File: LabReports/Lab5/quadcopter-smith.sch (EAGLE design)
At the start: 58 parts, among them J1 AVR_SPI_PRG_6NS, Q1 SI2302CDS, Q2 SI2302CDS, Q3 SI2302CDS, Q4 SI2302CDS, U1 ATMEGA128RFA1, U2 LSM9DS0-LGA24, Y1 16MHz

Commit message: Added grouping names and separators to schematic
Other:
- note added: "IMU (and bypass caps)"
- note added: "Microcontroller (and bypass caps, status LEDs)"
- note added: "Motor Controllers (and orientation LEDs)"
- note added: "Power Supply"
- note added: "Serial Headers"
- moved on the sheet: B1, C1, C10, C11, C12, C13, C14, C15, C16, C17, C18, C2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

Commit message: Beautified schematic
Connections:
- net VCC renamed VBAT
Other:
- note added: "Bypass Caps (place near supply pins)"
- note added: "IMU"
- note added: "Microcontroller"
- note added: "Motor Controllers"
- note added: "Orientation LEDs"
- note added: "Status LEDs"
- note added: "Trevor Smith and David Smith"
- note removed: "IMU (and bypass caps)"
- note removed: "Microcontroller (and bypass caps, status LEDs)"
- note removed: "Motor Controllers (and orientation LEDs)"
- moved on the sheet: B1, C1, C11, C12, C13, C14, C15, C16, C17, C18, C2, C3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

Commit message: Added design review of Dejun and Ryan
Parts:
- C3, C4: value 1mF -> 1uF
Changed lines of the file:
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@@
 <setting verticaltext="up"/>
 </settings>
-<grid distance="0.1" unitdist="inch" unit="inch" style="lines" multiple="1" display="no" altdistance="0.05" altunitdist="inch" altunit="inch"/>
+<grid distance="0.1" unitdist="inch" unit="inch" style="lines" multiple="1" display="no" altdistance="0.01" altunitdist="inch" altunit="inch"/>
 <layers>
 <layer number="1" name="Top" color="4" fill="1" visible="no" active="no"/>
@@
 <part name="GND1" library="Lab5" deviceset="GND" device=""/>
 <part name="GND2" library="Lab5" deviceset="GND" device=""/>
-<part name="C3" library="Lab5" deviceset="C-US" device="C0805" value="1mF"/>
-<part name="C4" library="Lab5" deviceset="C-US" device="C0805" value="1mF"/>
+<part name="C3" library="Lab5" deviceset="C-US" device="C0805" value="1uF"/>
+<part name="C4" library="Lab5" deviceset="C-US" device="C0805" value="1uF"/>
 <part name="GND3" library="Lab5" deviceset="GND" device=""/>
 <part name="GND4" library="Lab5" deviceset="GND" device=""/>

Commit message: modified schem after design review
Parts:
- removed C6, C7: JUMP, Lab5:C-USC0805
- added R12, R13, R14: 10k, Trevor-lab4:RESISTOR-0805
- added R15, R16: JUMP, Lab5:R-US_R0805
- LED1, LED2: value GREEN -> BLUE
- LED4, LED6: value (none) -> GREEN
- LED5, LED7: value (none) -> RED
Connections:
- removed net 3.3V: C10.1, C13.1, C17.1, C18.1, C9.1, R1.2, R10.2, R11.2, R4.2, R9.2, U$2.OUT, U1.DEVDD, U1.EVDD, U2.CS_G, U2.CS_XM, U2.DEN_G, U2.SDO_G/SA0_G, U2.SDO_XM/SA0_XM, U2.VDD_1, U2.VDD_2, U2.VDD_3, U2.VDD_IO
- new net 3V: C10.1, C13.1, C17.1, C18.1, C9.1, R1.2, R10.2, R11.2, R12.P$1, R13.P$1, R14.P$1, R4.2, R9.2, U$2.OUT, U1.DEVDD, U1.EVDD, U2.VDD_1, U2.VDD_2, U2.VDD_3, U2.VDD_IO
- new net N$27: R12.P$2, U2.CS_G
- new net N$28: R13.P$2, U2.CS_XM
- new net N$29: R14.P$2, U2.DEN_G
- net GND: now also U2.SDO_G/SA0_G, U2.SDO_XM/SA0_XM
- net N$5: now also R16.1; no longer C7.2
- net N$6: now also R15.1; no longer C6.2
- net N$7: now also R15.2; no longer C6.1
- net N$8: now also R16.2; no longer C7.1
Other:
- note added: "For easily identifying the orientation of the quadcopter when it is flying"

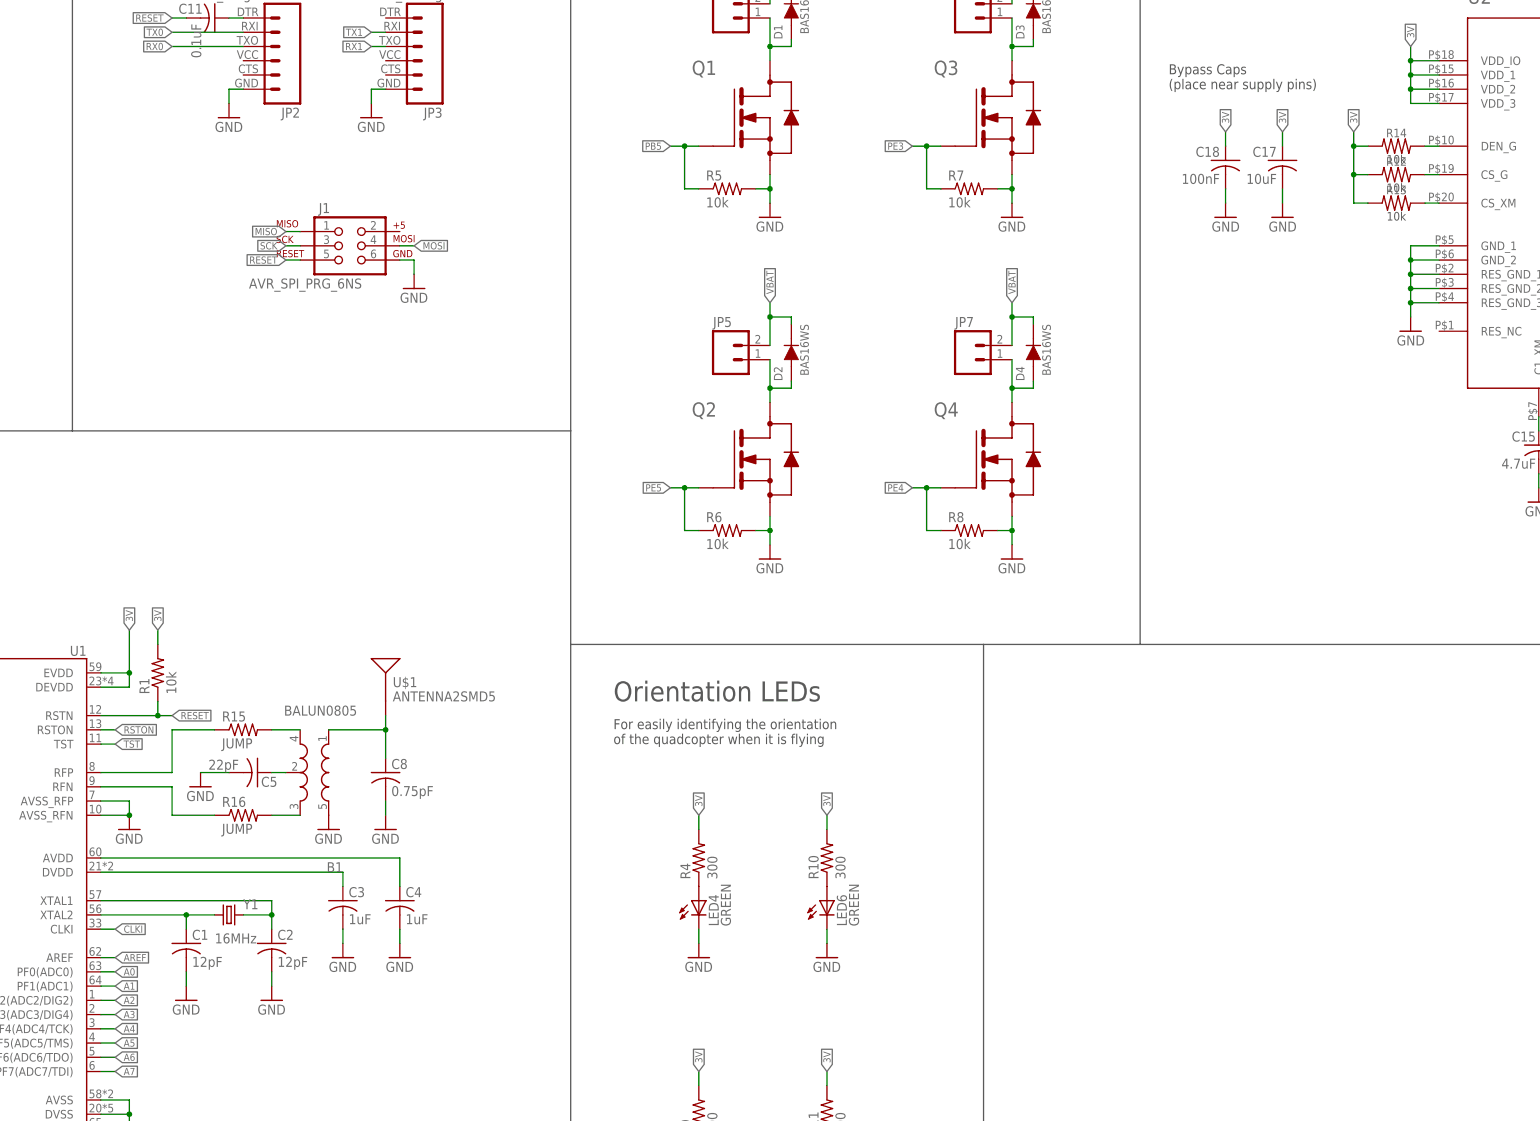
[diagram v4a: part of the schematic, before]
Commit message: removed jumpers on balun circuit, connected tst and clki on atmega to gnd
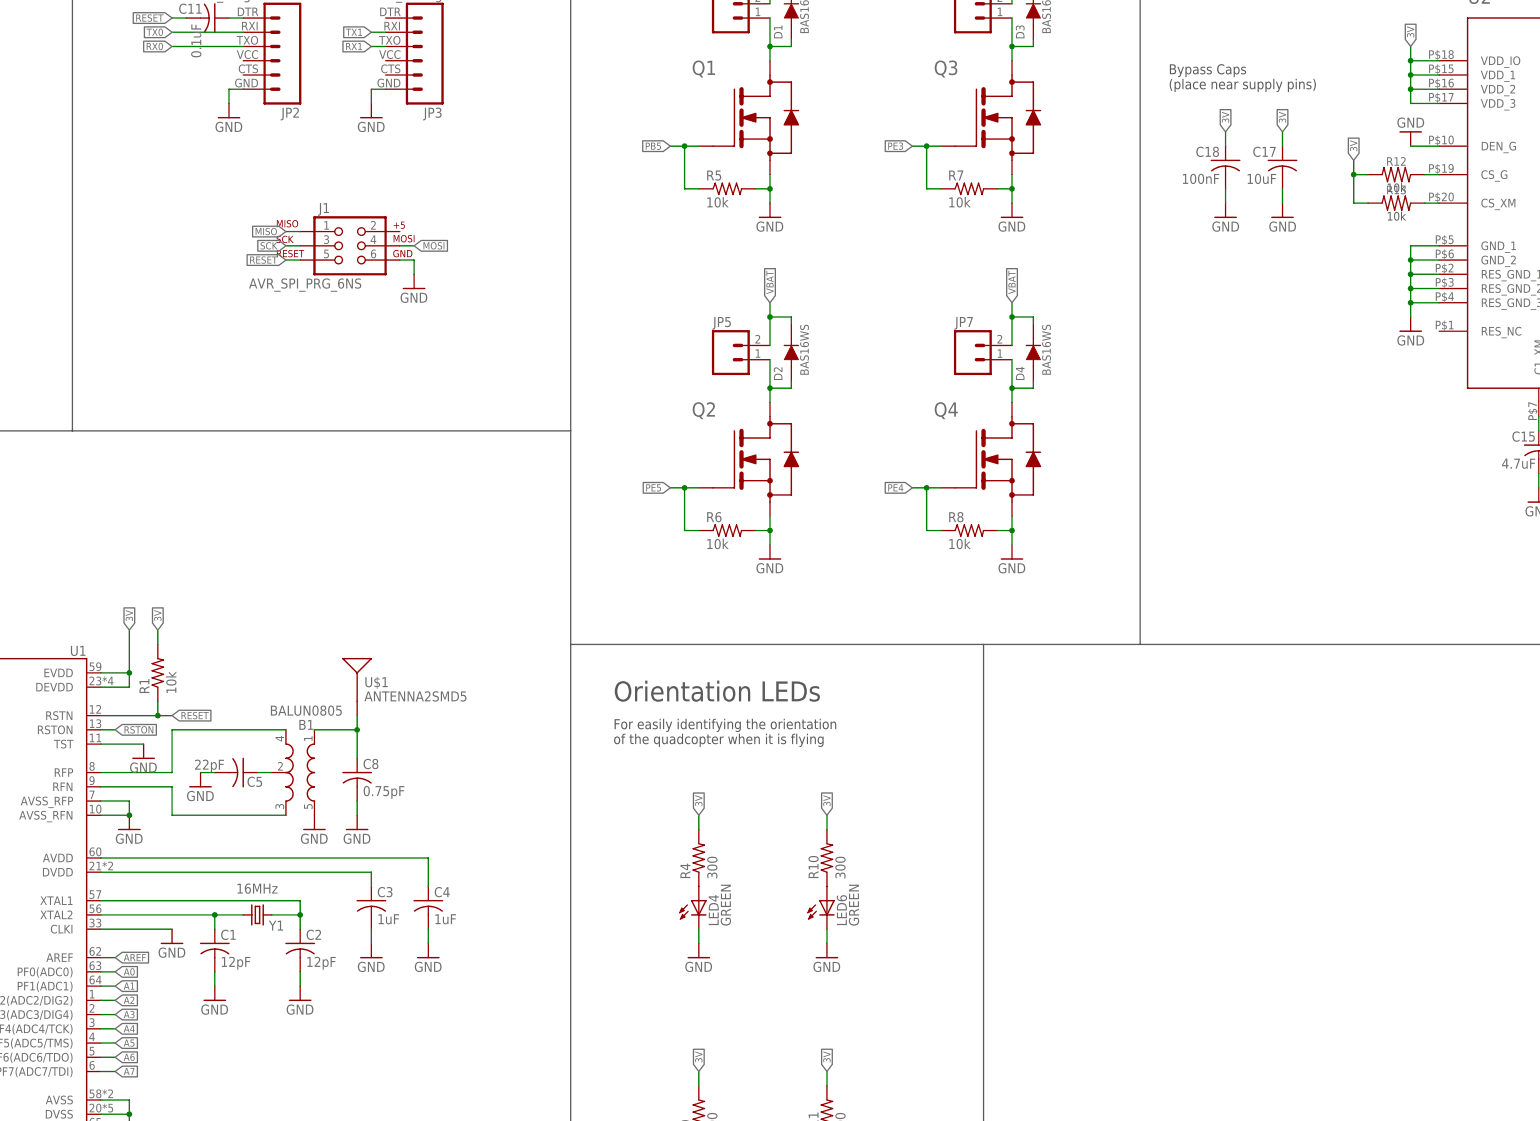
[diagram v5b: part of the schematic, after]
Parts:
- removed R14: 10k, Trevor-lab4:RESISTOR-0805
- removed R15, R16: JUMP, Lab5:R-US_R0805
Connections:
- removed net CLKI: U1.CLKI
- removed net N$29: R14.P$2, U2.DEN_G
- removed net N$7: B1.OUT1, R15.2
- removed net N$8: B1.OUT2, R16.2
- removed net TST: U1.TST
- net 3V: no longer R14.P$1
- net GND: now also U1.CLKI, U1.TST, U2.DEN_G
- net N$5: now also B1.OUT2; no longer R16.1
- net N$6: now also B1.OUT1; no longer R15.1
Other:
- moved on the sheet: B1, C1, C2, C3, C4, C5, C8, U$1, Y1

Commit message: square board initial layout
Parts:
- LED1: value BLUE -> ORANGE
- LED2: value BLUE -> YELLOW
- R10, R4: value 300 -> 30
- R11, R9: value 300 -> 100
- R12, R13: value 10k -> (none); device Trevor-lab4:RESISTOR-0805 -> Lab5:R-US_R0805
- R2, R3: value 300 -> 270
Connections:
- net 3V: now also R12.1, R13.1; no longer R10.2, R11.2, R12.P$1, R13.P$1, R4.2, R9.2
- net N$27: now also R12.2; no longer R12.P$2
- net N$28: now also R13.2; no longer R13.P$2
- net VBAT: now also R10.2, R11.2, R4.2, R9.2
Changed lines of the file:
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@@
 <part name="GND10" library="Lab5" deviceset="GND" device=""/>
 <part name="GND11" library="Lab5" deviceset="GND" device=""/>
-<part name="LED1" library="Lab5" deviceset="LED" device="CHIP-LED0805" value="BLUE"/>
-<part name="LED2" library="Lab5" deviceset="LED" device="CHIP-LED0805" value="BLUE"/>
-<part name="R2" library="Lab5" deviceset="R-US_" device="R0805" value="300"/>
-<part name="R3" library="Lab5" deviceset="R-US_" device="R0805" value="300"/>
+<part name="LED1" library="Lab5" deviceset="LED" device="CHIP-LED0805" value="ORANGE"/>
+<part name="LED2" library="Lab5" deviceset="LED" device="CHIP-LED0805" value="YELLOW"/>
+<part name="R2" library="Lab5" deviceset="R-US_" device="R0805" value="270"/>
+<part name="R3" library="Lab5" deviceset="R-US_" device="R0805" value="270"/>
 <part name="GND12" library="Lab5" deviceset="GND" device=""/>
 <part name="GND13" library="Lab5" deviceset="GND" device=""/>
@@
 <part name="LED6" library="Lab5" deviceset="LED" device="CHIP-LED0805" value="GREEN"/>
 <part name="LED7" library="Lab5" deviceset="LED" device="CHIP-LED0805" value="RED"/>
-<part name="R4" library="Lab5" deviceset="R-US_" device="R0805" value="300"/>
-<part name="R9" library="Lab5" deviceset="R-US_" device="R0805" value="300"/>
-<part name="R10" library="Lab5" deviceset="R-US_" device="R0805" value="300"/>
-<part name="R11" library="Lab5" deviceset="R-US_" device="R0805" value="300"/>
+<part name="R4" library="Lab5" deviceset="R-US_" device="R0805" value="30"/>
+<part name="R9" library="Lab5" deviceset="R-US_" device="R0805" value="100"/>
+<part name="R10" library="Lab5" deviceset="R-US_" device="R0805" value="30"/>
+<part name="R11" library="Lab5" deviceset="R-US_" device="R0805" value="100"/>
 <part name="GND19" library="Lab5" deviceset="GND" device=""/>
 <part name="GND31" library="Lab5" deviceset="GND" device=""/>
 <part name="GND32" library="Lab5" deviceset="GND" device=""/>
 <part name="GND33" library="Lab5" deviceset="GND" device=""/>
-<part name="R12" library="Trevor-lab4" deviceset="RESISTOR" device="-0805" value="10k"/>
-<part name="R13" library="Trevor-lab4" deviceset="RESISTOR" device="-0805" value="10k"/>
 <part name="GND34" library="Lab5" deviceset="GND" device=""/>
 <part name="GND35" library="Lab5" deviceset="GND" device=""/>
 <part name="GND36" library="Lab5" deviceset="GND" device=""/>
 <part name="GND37" library="Lab5" deviceset="GND" device=""/>
+<part name="R12" library="Lab5" deviceset="R-US_" device="R0805"/>
+<part name="R13" library="Lab5" deviceset="R-US_" device="R0805"/>
 </parts>
 <sheets>
@@
 <instance part="GND32" gate="1" x="254" y="76.2"/>
 <instance part="GND33" gate="1" x="254" y="30.48"/>
-<instance part="R12" gate="G$1" x="355.6" y="215.9"/>
-<instance part="R13" gate="G$1" x="355.6" y="210.82"/>
 <instance part="GND34" gate="1" x="416.56" y="215.9"/>
 <instance part="GND35" gate="1" x="137.16" y="78.74"/>
 <instance part="GND36" gate="1" x="132.08" y="111.76"/>
 <instance part="GND37" gate="1" x="358.14" y="223.52" rot="R180"/>
+<instance part="R12" gate="G$1" x="355.6" y="215.9"/>
+<instance part="R13" gate="G$1" x="355.6" y="210.82"/>
 </instances>
 <busses>
@@
 </segment>
 <segment>
-<pinref part="R4" gate="G$1" pin="2"/>
-<wire x1="231.14" y1="101.6" x2="231.14" y2="99.06" width="0.1524" layer="91"/>
-<label x="231.14" y="101.6" size="1.27" layer="95" rot="R90" xref="yes"/>
-</segment>
-<segment>
-<pinref part="R10" gate="G$1" pin="2"/>
-<wire x1="254" y1="101.6" x2="254" y2="99.06" width="0.1524" layer="91"/>
-<label x="254" y="101.6" size="1.27" layer="95" rot="R90" xref="yes"/>
-</segment>
-<segment>
-<pinref part="R9" gate="G$1" pin="2"/>
-<wire x1="231.14" y1="53.34" x2="231.14" y2="55.88" width="0.1524" layer="91"/>
-<label x="231.14" y="55.88" size="1.27" layer="95" rot="R90" xref="yes"/>
-</segment>
-<segment>
-<pinref part="R11" gate="G$1" pin="2"/>
-<wire x1="254" y1="53.34" x2="254" y2="55.88" width="0.1524" layer="91"/>
-<label x="254" y="55.88" size="1.27" layer="95" rot="R90" xref="yes"/>
-</segment>
-<segment>
-<pinref part="R13" gate="G$1" pin="P$1"/>
 <wire x1="350.52" y1="210.82" x2="347.98" y2="210.82" width="0.1524" layer="91"/>
 <wire x1="347.98" y1="210.82" x2="347.98" y2="215.9" width="0.1524" layer="91"/>
-<pinref part="R12" gate="G$1" pin="P$1"/>
 <wire x1="347.98" y1="215.9" x2="347.98" y2="218.44" width="0.1524" layer="91"/>
 <wire x1="347.98" y1="215.9" x2="350.52" y2="215.9" width="0.1524" layer="91"/>
 <junction x="347.98" y="215.9"/>
 <label x="347.98" y="218.44" size="1.27" layer="95" rot="R90" xref="yes"/>
+<pinref part="R12" gate="G$1" pin="1"/>
+<pinref part="R13" gate="G$1" pin="1"/>
 </segment>
 <segment>
@@
 <junction x="287.02" y="190.5"/>
 </segment>
+<segment>
+<pinref part="R4" gate="G$1" pin="2"/>
+<wire x1="231.14" y1="101.6" x2="231.14" y2="99.06" width="0.1524" layer="91"/>
+<label x="231.14" y="101.6" size="1.27" layer="95" rot="R90" xref="yes"/>
+</segment>
+<segment>
+<pinref part="R10" gate="G$1" pin="2"/>
+<wire x1="254" y1="101.6" x2="254" y2="99.06" width="0.1524" layer="91"/>
+<label x="254" y="101.6" size="1.27" layer="95" rot="R90" xref="yes"/>
+</segment>
+<segment>
+<pinref part="R9" gate="G$1" pin="2"/>
+<wire x1="231.14" y1="53.34" x2="231.14" y2="55.88" width="0.1524" layer="91"/>
+<label x="231.14" y="55.88" size="1.27" layer="95" rot="R90" xref="yes"/>
+</segment>
+<segment>
+<pinref part="R11" gate="G$1" pin="2"/>
+<wire x1="254" y1="53.34" x2="254" y2="55.88" width="0.1524" layer="91"/>
+<label x="254" y="55.88" size="1.27" layer="95" rot="R90" xref="yes"/>
+</segment>
 </net>
 <net name="N$16" class="0">
@@
 <segment>
 <pinref part="U2" gate="G$1" pin="CS_G"/>
-<pinref part="R12" gate="G$1" pin="P$2"/>
 <wire x1="360.68" y1="215.9" x2="363.22" y2="215.9" width="0.1524" layer="91"/>
+<pinref part="R12" gate="G$1" pin="2"/>
 </segment>
 </net>
@@
 <segment>
 <pinref part="U2" gate="G$1" pin="CS_XM"/>
-<pinref part="R13" gate="G$1" pin="P$2"/>
 <wire x1="360.68" y1="210.82" x2="363.22" y2="210.82" width="0.1524" layer="91"/>
-</segment>
-</net>
+<pinref part="R13" gate="G$1" pin="2"/>
+</segment>
+</net>

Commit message: shrink, route, modified some parts in Lab5.lbr
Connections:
- net GND: no longer U1.PADDLE
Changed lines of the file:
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@@
 </segment>
 </net>
-<net name="GND" class="1">
+<net name="GND" class="0">
 <segment>
 <pinref part="C1" gate="G$1" pin="2"/>
@@
 <wire x1="129.54" y1="50.8" x2="129.54" y2="48.26" width="0.1524" layer="91"/>
 <pinref part="U1" gate="G$1" pin="DVSS"/>
-<wire x1="129.54" y1="48.26" x2="129.54" y2="45.72" width="0.1524" layer="91"/>
-<wire x1="129.54" y1="45.72" x2="129.54" y2="43.18" width="0.1524" layer="91"/>
+<wire x1="129.54" y1="48.26" x2="129.54" y2="43.18" width="0.1524" layer="91"/>
 <wire x1="124.46" y1="48.26" x2="129.54" y2="48.26" width="0.1524" layer="91"/>
-<pinref part="U1" gate="G$1" pin="PADDLE"/>
-<wire x1="124.46" y1="45.72" x2="129.54" y2="45.72" width="0.1524" layer="91"/>
 <junction x="129.54" y="48.26"/>
-<junction x="129.54" y="45.72"/>
 </segment>
 <segment>
@@
 </segment>
 </net>
-<net name="N$9" class="2">
+<net name="N$9" class="0">
 <segment>
 <pinref part="B1" gate="G$1" pin="IN"/>
@@
 </segment>
 </net>
-<net name="VBAT" class="1">
+<net name="VBAT" class="0">
 <segment>
 <pinref part="U$2" gate="G$1" pin="IN"/>
@@
 </segment>
 </net>
-<net name="N$14" class="1">
+<net name="N$14" class="0">
 <segment>
 <pinref part="LED4" gate="G$1" pin="A"/>
